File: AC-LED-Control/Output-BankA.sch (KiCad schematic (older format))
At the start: 58 parts

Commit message: Changed up isolation scheme and added BOM
Instead of isolating each of the TRIAC channels individually,
I changed it so the system uses an isolated power supply and isolates
itself from I2C as well.

Basic BOM was started as well.
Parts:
- removed R? (x16): 56, symbol R
- removed U? (x2): LTV-846S, symbol LTV-846S
- R? (x8): value 660 -> 100
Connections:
- net labels added: AC_LOAD-E, AC_LOAD-F, AC_LOAD-G, AC_LOAD-H
- net labels removed: GND
- wire segments 152 -> 83
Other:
- moved on the sheet: R?

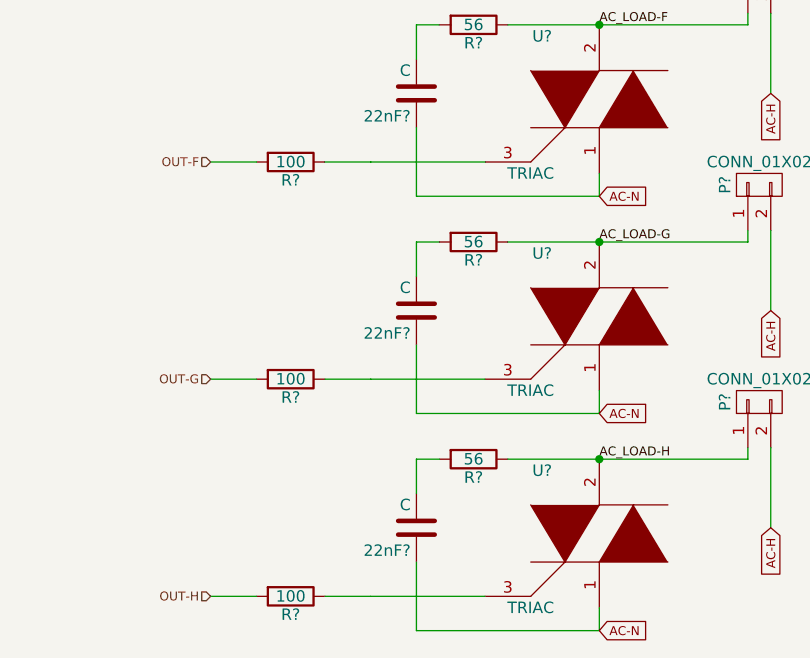
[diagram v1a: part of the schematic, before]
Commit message: Modified some values for finding components
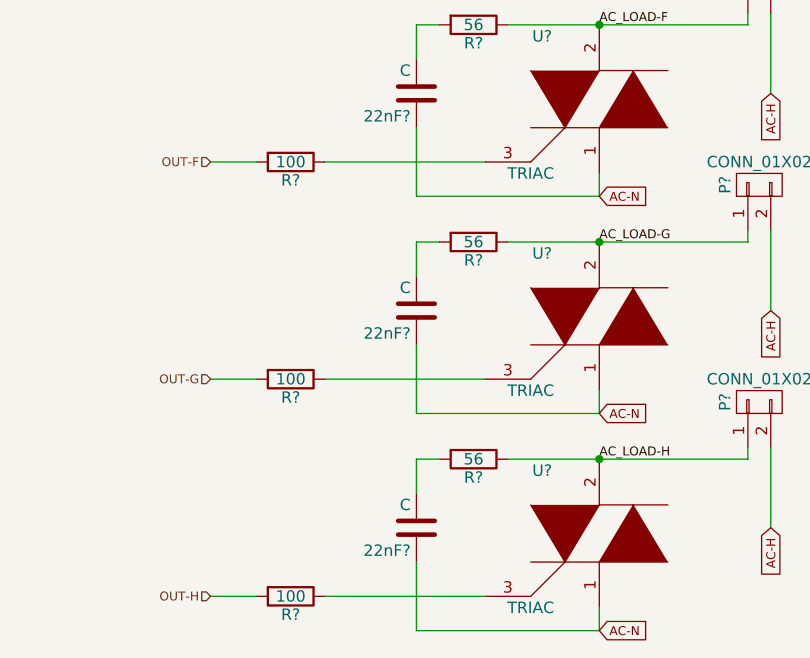
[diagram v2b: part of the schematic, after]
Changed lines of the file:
@@
 $EndComp
 Wire Wire Line
-	8000 2600 8200 2600
+	8000 2600 8700 2600
 Wire Wire Line
-	8000 3550 8200 3550
+	8000 3550 8700 3550
 Wire Wire Line
-	8000 4500 8200 4500
+	8000 4500 8700 4500
 Wire Wire Line
 	7700 2600 7500 2600
@@
 	8400 2000 8400 2150
 Wire Wire Line
-	8700 2600 8200 2600
-Wire Wire Line
 	9200 2750 9200 2650
 Wire Wire Line
@@
 Wire Wire Line
 	8400 2950 8400 3100
-Wire Wire Line
-	8700 3550 8200 3550
 Wire Wire Line
 	9200 3700 9200 3600
@@
 	8400 3900 8400 4050
 Wire Wire Line
-	8700 4500 8200 4500
-Wire Wire Line
 	9200 4650 9200 4550

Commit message: Saved state on july 23
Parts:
- removed 22nF (x3), 22nF?: C, symbol C
- removed P? (x4): CONN_01X02, symbol CONN_01X02
- removed R? (x3): 56, symbol R
- removed U? (x4): TRIAC, symbol TRIAC
- added 22nF201, 22nF205, 22nF206, 22nF207: C, symbol C
- added P201, P202, P205, P208: CONN_01X02, symbol CONN_01X02
- added R201, R205, R213: 56, symbol R
- added U201, U202, U203, U207: TRIAC, symbol TRIAC
- gave numbers to parts that had none: 24
- renumbered 22nF to 22nF203
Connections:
- net AC-H: now also P201.2 (P2), P202.2 (P2), P205.2 (P2), P208.2 (P2)
- net AC-N: now also 22nF201.1, 22nF205.1, 22nF206.1, 22nF207.1, U201.1, U202.1, U203.1, U207.1
- net AC_LOAD-A: now also P201.1 (P1), R201.1, U201.2
- net AC_LOAD-B: now also R205.1, U203.2
- net AC_LOAD-C: now also P205.1 (P1)
- net AC_LOAD-D: now also R213.1, U207.2
- net AC_LOAD-E: now also P202.1 (P1), U202.2
- net AC_LOAD-H: now also P208.1 (P1)
- net at R203.1: now also U201.3
- net at R207.1: now also U203.3
- net at R215.1: now also U207.3
- net at 22nF203.2: now also R205.2
- net at R209.2: now also 22nF205.2
- net at R204.1: now also U202.3
- net at R210.2: now also 22nF206.2
- new net: 22nF201.2, R201.2
- new net: 22nF207.2, R213.2

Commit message: Finished final associations and tweaks
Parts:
- removed P201, P202, P203, P204, P205, P206, P207, P208: CONN_01X02, symbol CONN_01X02
- added J201, J202, J203, J204, J205, J206, J207, J208: Conn_01x02, Connectors_OnShore:OSTTC022162, symbol Conn_01x02
- C201: renamed from 22nF201; value C -> 22n; footprint (none) -> Capacitors_SMD:C_0603_HandSoldering
- C202: renamed from 22nF202; value C -> 22n; footprint (none) -> Capacitors_SMD:C_0603_HandSoldering
- C203: renamed from 22nF203; value C -> 22n; footprint (none) -> Capacitors_SMD:C_0603_HandSoldering
- C204: renamed from 22nF204; value C -> 22n; footprint (none) -> Capacitors_SMD:C_0603_HandSoldering
- C205: renamed from 22nF205; value C -> 22n; footprint (none) -> Capacitors_SMD:C_0603_HandSoldering
- C206: renamed from 22nF206; value C -> 22n; footprint (none) -> Capacitors_SMD:C_0603_HandSoldering
- C207: renamed from 22nF207; value C -> 22n; footprint (none) -> Capacitors_SMD:C_0603_HandSoldering
- C208: renamed from 22nF208; value C -> 22n; footprint (none) -> Capacitors_SMD:C_0603_HandSoldering
- R201, R202, R203, R204, R205, R206, R207, R208, R209, R210, R211, R212, R213, R214, R215, R216: footprint (none) -> Resistors_SMD:R_0603_HandSoldering
- U201, U202, U203, U204, U205, U206, U207, U208: footprint (none) -> Power-Packages:DPAK
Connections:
- net AC-H: now also J201.2 (Pin_2), J202.2 (Pin_2), J203.2 (Pin_2), J204.2 (Pin_2), J205.2 (Pin_2), J206.2 (Pin_2), J207.2 (Pin_2), J208.2 (Pin_2)
- net AC_LOAD-A: now also J201.1 (Pin_1)
- net AC_LOAD-B: now also J203.1 (Pin_1)
- net AC_LOAD-C: now also J205.1 (Pin_1)
- net AC_LOAD-D: now also J207.1 (Pin_1)
- net AC_LOAD-E: now also J202.1 (Pin_1)
- net AC_LOAD-F: now also J204.1 (Pin_1)
- net AC_LOAD-G: now also J206.1 (Pin_1)
- net AC_LOAD-H: now also J208.1 (Pin_1)

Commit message: Changed TRIAC from DPAK part to T0-202-3 part.
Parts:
- U201, U202, U203, U204, U205, U206, U207, U208: footprint Power-Packages:DPAK -> Power-Packages:TO-202-3-Vertical
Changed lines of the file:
@@
 F 0 "U201" H 4050 1800 50  0000 C CNN
 F 1 "TRIAC" H 4000 1200 50  0000 C CNN
-F 2 "Power-Packages:DPAK" H 4300 1450 50  0001 C CNN
+F 2 "Power-Packages:TO-202-3-Vertical" H 4300 1450 50  0001 C CNN
 F 3 "" H 4300 1450 50  0000 C CNN
 	1    4300 1450
@@
 F 0 "U203" H 4050 2750 50  0000 C CNN
 F 1 "TRIAC" H 4000 2150 50  0000 C CNN
-F 2 "Power-Packages:DPAK" H 4300 2400 50  0001 C CNN
+F 2 "Power-Packages:TO-202-3-Vertical" H 4300 2400 50  0001 C CNN
 F 3 "" H 4300 2400 50  0000 C CNN
 	1    4300 2400
@@
 F 0 "U205" H 4050 3700 50  0000 C CNN
 F 1 "TRIAC" H 4000 3100 50  0000 C CNN
-F 2 "Power-Packages:DPAK" H 4300 3350 50  0001 C CNN
+F 2 "Power-Packages:TO-202-3-Vertical" H 4300 3350 50  0001 C CNN
 F 3 "" H 4300 3350 50  0000 C CNN
 	1    4300 3350
@@
 F 0 "U207" H 4050 4650 50  0000 C CNN
 F 1 "TRIAC" H 4000 4050 50  0000 C CNN
-F 2 "Power-Packages:DPAK" H 4300 4300 50  0001 C CNN
+F 2 "Power-Packages:TO-202-3-Vertical" H 4300 4300 50  0001 C CNN
 F 3 "" H 4300 4300 50  0000 C CNN
 	1    4300 4300
@@
 F 0 "U202" H 8950 1800 50  0000 C CNN
 F 1 "TRIAC" H 8900 1200 50  0000 C CNN
-F 2 "Power-Packages:DPAK" H 9200 1450 50  0001 C CNN
+F 2 "Power-Packages:TO-202-3-Vertical" H 9200 1450 50  0001 C CNN
 F 3 "" H 9200 1450 50  0000 C CNN
 	1    9200 1450
@@
 F 0 "U204" H 8950 2750 50  0000 C CNN
 F 1 "TRIAC" H 8900 2150 50  0000 C CNN
-F 2 "Power-Packages:DPAK" H 9200 2400 50  0001 C CNN
+F 2 "Power-Packages:TO-202-3-Vertical" H 9200 2400 50  0001 C CNN
 F 3 "" H 9200 2400 50  0000 C CNN
 	1    9200 2400
@@
 F 0 "U206" H 8950 3700 50  0000 C CNN
 F 1 "TRIAC" H 8900 3100 50  0000 C CNN
-F 2 "Power-Packages:DPAK" H 9200 3350 50  0001 C CNN
+F 2 "Power-Packages:TO-202-3-Vertical" H 9200 3350 50  0001 C CNN
 F 3 "" H 9200 3350 50  0000 C CNN
 	1    9200 3350
@@
 F 0 "U208" H 8950 4650 50  0000 C CNN
 F 1 "TRIAC" H 8900 4050 50  0000 C CNN
-F 2 "Power-Packages:DPAK" H 9200 4300 50  0001 C CNN
+F 2 "Power-Packages:TO-202-3-Vertical" H 9200 4300 50  0001 C CNN
 F 3 "" H 9200 4300 50  0000 C CNN
 	1    9200 4300

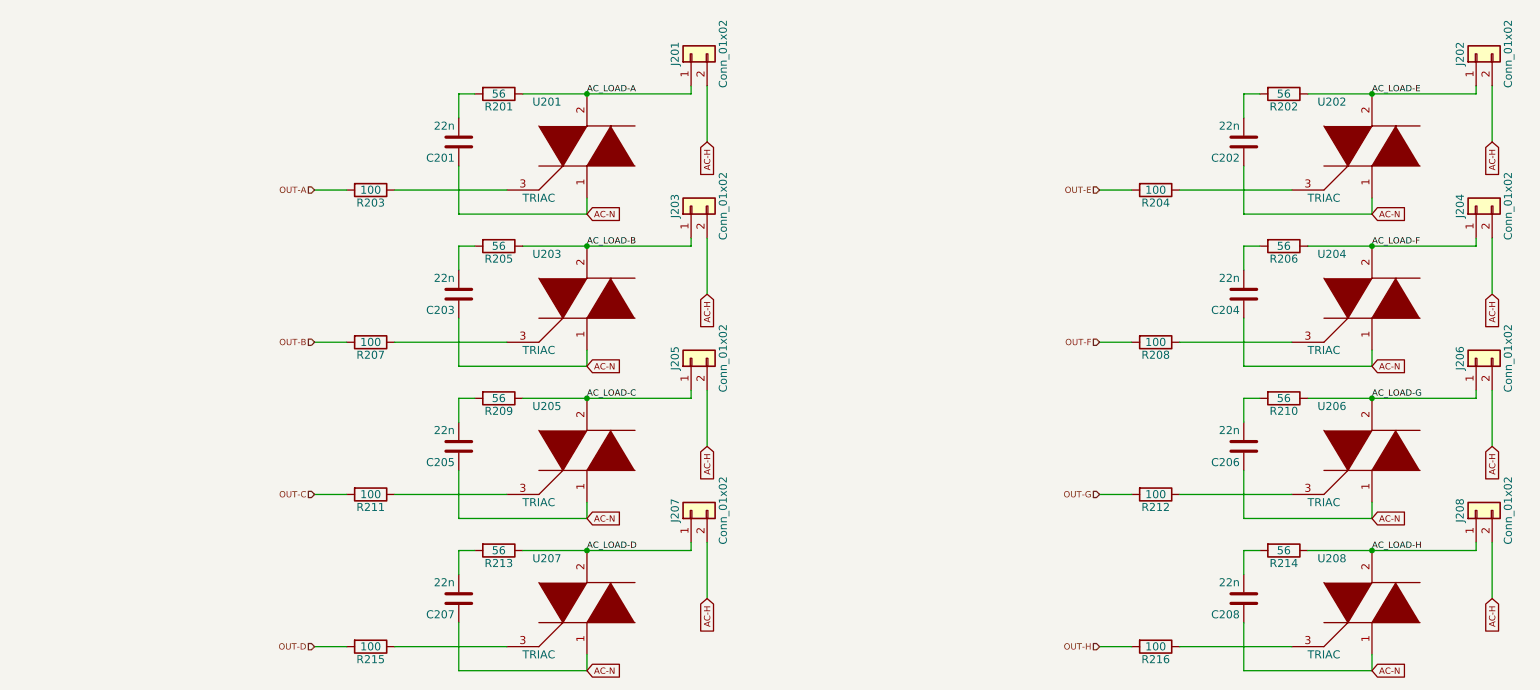
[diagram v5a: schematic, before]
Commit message: Lots of layout + added a diode.
I realised that the power regulator might need protection from the 3v3
line on the programming header.
Added a diode just in case.
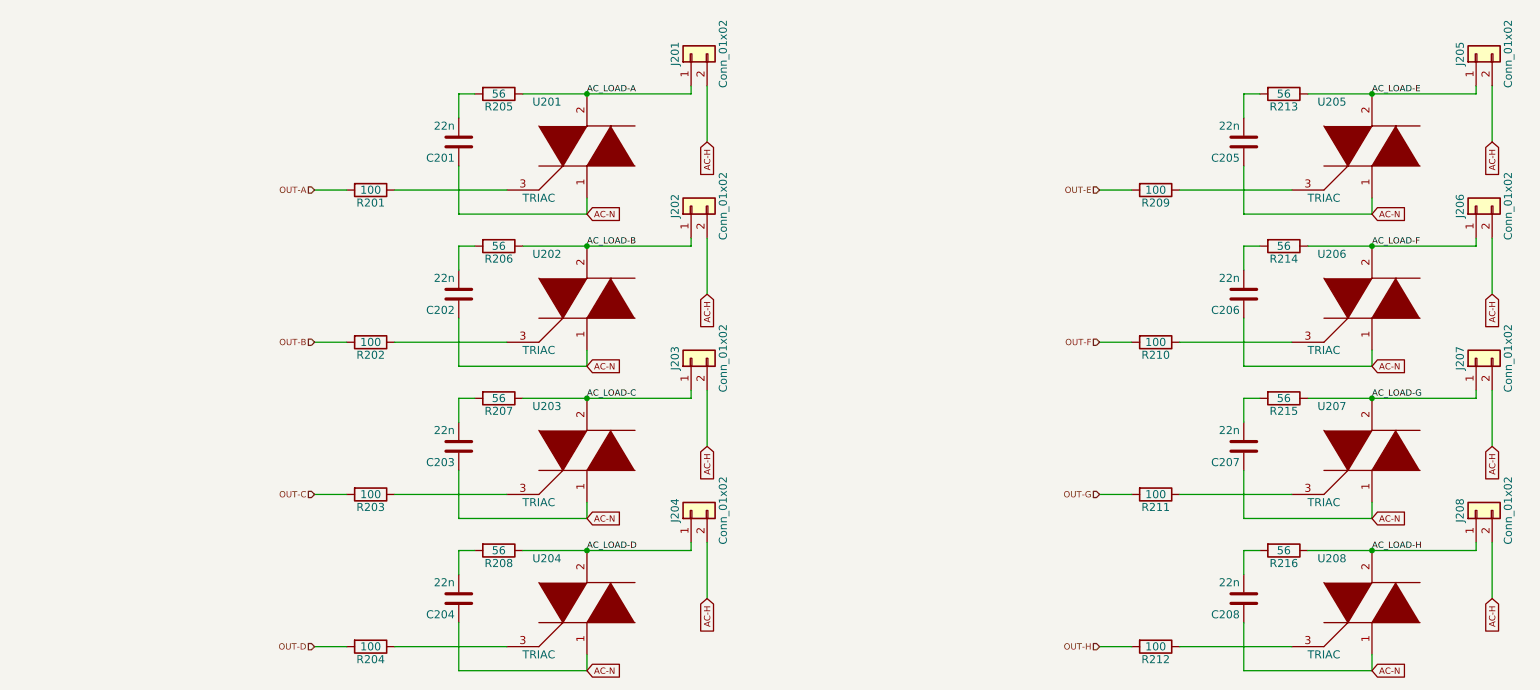
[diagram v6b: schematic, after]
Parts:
- renumbered C203 to C202, C205 to C203, C207 to C204, C202 to C205, C204 to C206, C206 to C207, J203 to J202, J205 to J203, J207 to J204, J202 to J205, J204 to J206, J206 to J207, R203 to R201, R207 to R202, R211 to R203, R215 to R204, R201 to R205, R205 to R206, R209 to R207, R213 to R208, R204 to R209, R208 to R210, R212 to R211, R216 to R212, R202 to R213, R206 to R214, R210 to R215, R214 to R216, U203 to U202, U205 to U203, U207 to U204, U202 to U205, U204 to U206, U206 to U207
